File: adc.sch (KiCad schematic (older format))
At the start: 19 parts, among them J15 Conn_01x04_Male, U22 AD7960BCPZ-RL7, U23 OPA325

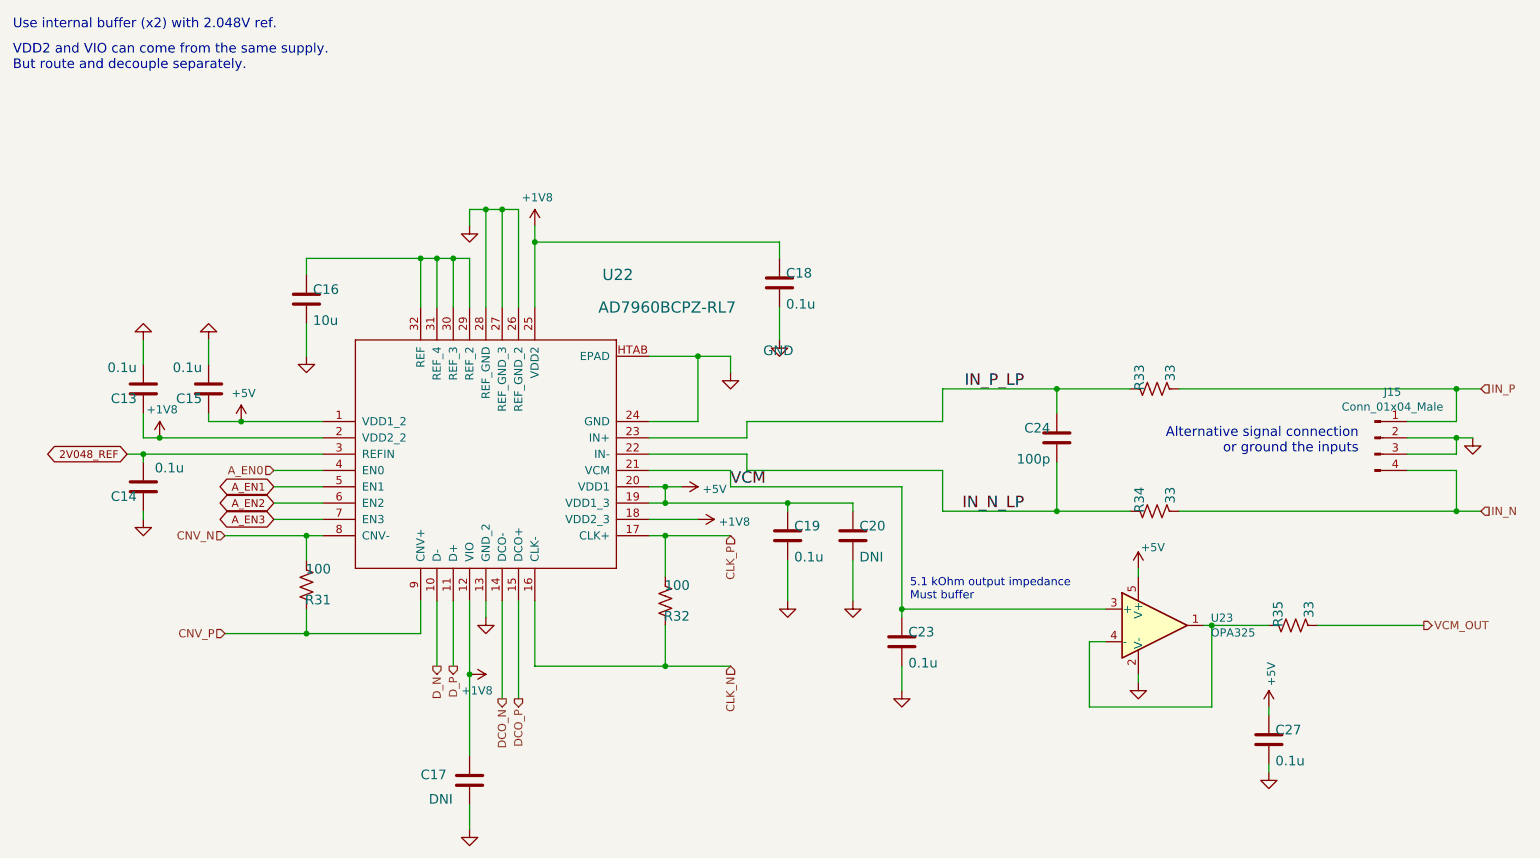
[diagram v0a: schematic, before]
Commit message: moved DCO 7960 signals to dedicated input clock routes
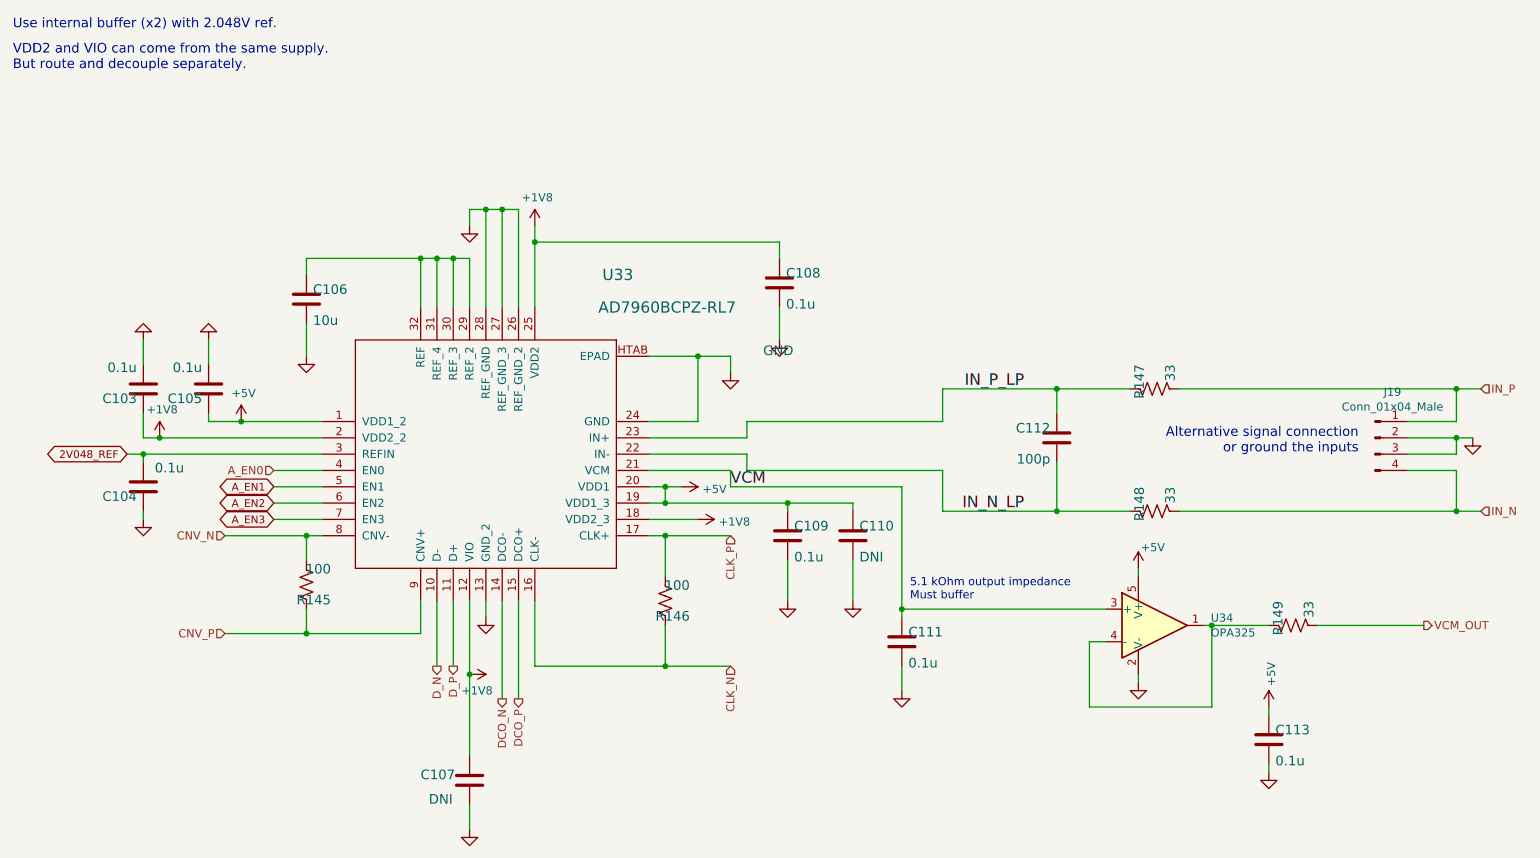
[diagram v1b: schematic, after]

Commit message: added Unique ID chip
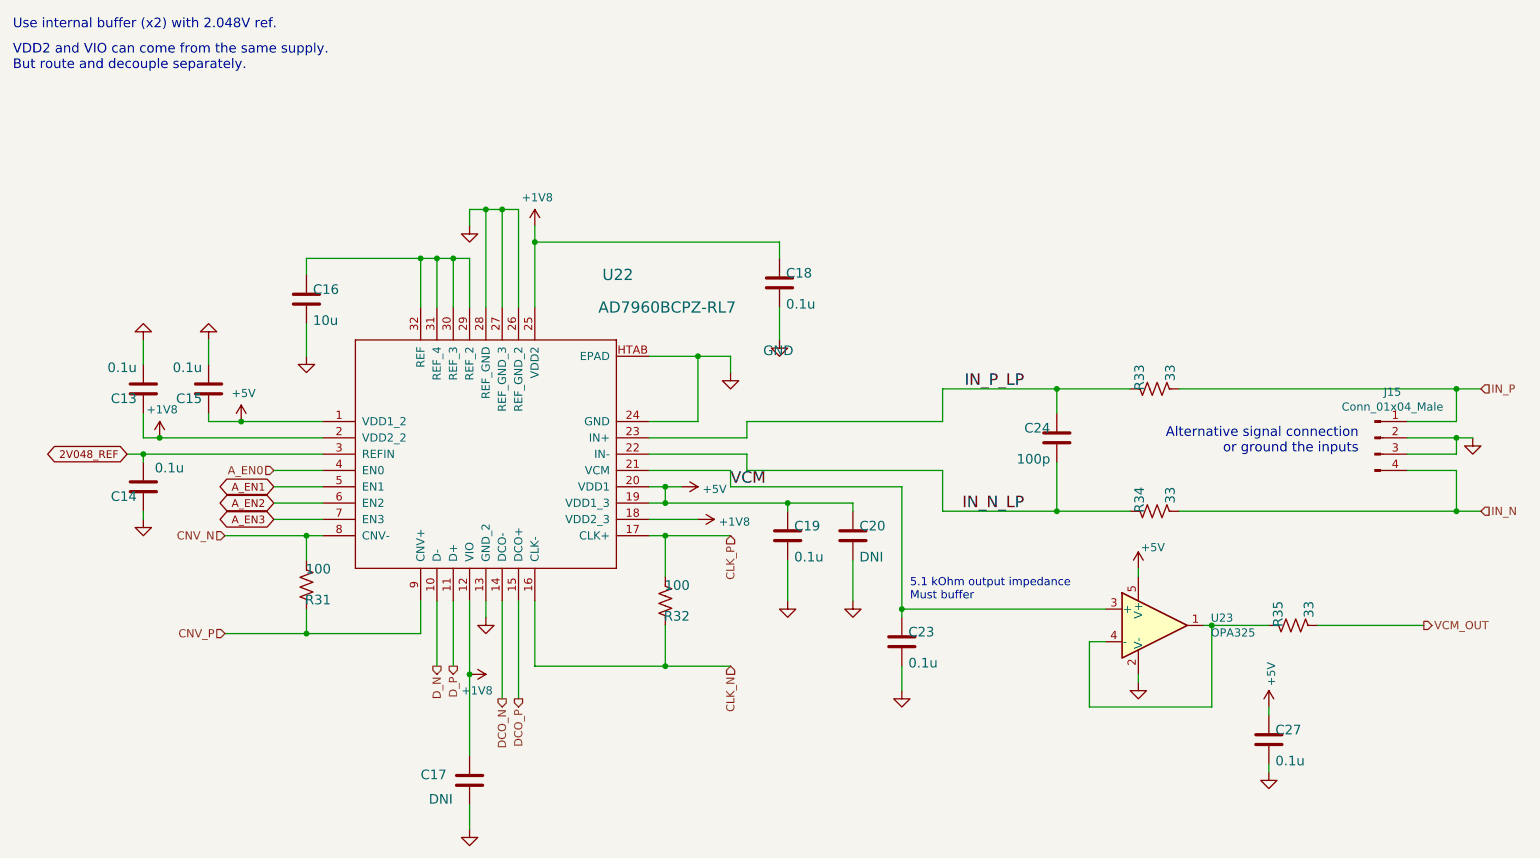
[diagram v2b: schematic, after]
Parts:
- J15: footprint (none) -> Connector_PinHeader_2.54mm:PinHeader_1x04_P2.54mm_Vertical_SMD_Pin1Left; Manf# (none) -> 54201-G0804LF
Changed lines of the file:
@@
 $Descr A 11000 8500
 encoding utf-8
-Sheet 10 18
+Sheet 6 18
 Title ""
 Date ""
@@
 AR Path="/60BF7757/B0DC2316" Ref="C69"  Part="1"
 AR Path="/60C1F416/B0DC2316" Ref="C112"  Part="1"
-F 0 "C112" H 7090 3725 59  0000 L BNN
+F 0 "C24" H 7090 3725 59  0000 L BNN
 F 1 "100p" H 7090 3535 59  0000 L BNN
 F 2 "Capacitor_SMD:C_0603_1608Metric" H 7050 3700 50  0001 C CNN
@@
 AR Path="/60BF7757/B996151F" Ref="R140"  Part="1"
 AR Path="/60C1F416/B996151F" Ref="R145"  Part="1"
-F 0 "R145" H 2300 4659 59  0000 L BNN
+F 0 "R31" H 2300 4659 59  0000 L BNN
 F 1 "100" H 2300 4470 59  0000 L BNN
 F 2 "Resistor_SMD:R_0603_1608Metric" H 2450 4600 50  0001 C CNN
@@
 AR Path="/60BF7757/56DFCCD0" Ref="C65"  Part="1"
 AR Path="/60C1F416/56DFCCD0" Ref="C108"  Part="1"
-F 0 "C108" H 5390 2775 59  0000 L BNN
+F 0 "C18" H 5390 2775 59  0000 L BNN
 F 1 "0.1u" H 5390 2585 59  0000 L BNN
 F 2 "Capacitor_SMD:C_0603_1608Metric" H 5350 2750 50  0001 C CNN
@@
 AR Path="/60BF7757/BF33D434" Ref="R141"  Part="1"
 AR Path="/60C1F416/BF33D434" Ref="R146"  Part="1"
-F 0 "R146" H 4500 4759 59  0000 L BNN
+F 0 "R32" H 4500 4759 59  0000 L BNN
 F 1 "100" H 4500 4570 59  0000 L BNN
 F 2 "Resistor_SMD:R_0603_1608Metric" H 4650 4700 50  0001 C CNN
@@
 AR Path="/60BF7757/C9238E33" Ref="C66"  Part="1"
 AR Path="/60C1F416/C9238E33" Ref="C109"  Part="1"
-F 0 "C109" H 5440 4325 59  0000 L BNN
+F 0 "C19" H 5440 4325 59  0000 L BNN
 F 1 "0.1u" H 5440 4135 59  0000 L BNN
 F 2 "Capacitor_SMD:C_0603_1608Metric" H 5400 4300 50  0001 C CNN
@@
 AR Path="/60BF7757/E612D2BB" Ref="C67"  Part="1"
 AR Path="/60C1F416/E612D2BB" Ref="C110"  Part="1"
-F 0 "C110" H 5840 4325 59  0000 L BNN
+F 0 "C20" H 5840 4325 59  0000 L BNN
 F 1 "DNI" H 5840 4135 59  0000 L BNN
 F 2 "Capacitor_SMD:C_0603_1608Metric" H 5800 4300 50  0001 C CNN
@@
 AR Path="/60BF7757/1FADEAAB" Ref="C60"  Part="1"
 AR Path="/60C1F416/1FADEAAB" Ref="C103"  Part="1"
-F 0 "C103" H 1490 3425 59  0000 L BNN
+F 0 "C13" H 1490 3425 59  0000 L BNN
 F 1 "0.1u" H 1490 3235 59  0000 L BNN
 F 2 "Capacitor_SMD:C_0603_1608Metric" H 1450 3400 50  0001 C CNN
@@
 AR Path="/60BF7757/9D5B9004" Ref="C62"  Part="1"
 AR Path="/60C1F416/9D5B9004" Ref="C105"  Part="1"
-F 0 "C105" H 1890 3425 59  0000 L BNN
+F 0 "C15" H 1890 3425 59  0000 L BNN
 F 1 "0.1u" H 1890 3235 59  0000 L BNN
 F 2 "Capacitor_SMD:C_0603_1608Metric" H 1850 3400 50  0001 C CNN
@@
 AR Path="/60BF7757/87DF8B8E" Ref="R142"  Part="1"
 AR Path="/60C1F416/87DF8B8E" Ref="R147"  Part="1"
-F 0 "R147" H 7500 3459 59  0000 L BNN
+F 0 "R33" H 7500 3459 59  0000 L BNN
 F 1 "33" H 7500 3270 59  0000 L BNN
 F 2 "Resistor_SMD:R_0603_1608Metric" H 7650 3400 50  0001 C CNN
@@
 AR Path="/60BF7757/BFC3FA38" Ref="R143"  Part="1"
 AR Path="/60C1F416/BFC3FA38" Ref="R148"  Part="1"
-F 0 "R148" H 7500 4209 59  0000 L BNN
+F 0 "R34" H 7500 4209 59  0000 L BNN
 F 1 "33" H 7500 4020 59  0000 L BNN
 F 2 "Resistor_SMD:R_0603_1608Metric" H 7650 4150 50  0001 C CNN
@@
 AR Path="/60BF7757/E8572435" Ref="C64"  Part="1"
 AR Path="/60C1F416/E8572435" Ref="C107"  Part="1"
-F 0 "C107" H 3150 5800 59  0000 L BNN
+F 0 "C17" H 3150 5800 59  0000 L BNN
 F 1 "DNI" H 3200 5650 59  0000 L BNN
 F 2 "Capacitor_SMD:C_0603_1608Metric" H 3450 5800 50  0001 C CNN
@@
 AR Path="/60BF7757/70C280EF" Ref="U31"  Part="1"
 AR Path="/60C1F416/70C280EF" Ref="U33"  Part="1"
-F 0 "U33" H 4264 4859 69  0000 L BNN
+F 0 "U22" H 4264 4859 69  0000 L BNN
 F 1 "AD7960BCPZ-RL7" H 4239 4659 69  0000 L BNN
 F 2 "adc_dac_v1:CP_32_7" H 3550 3800 50  0001 C CNN
@@
 AR Path="/60BF7757/32508C8E" Ref="C63"  Part="1"
 AR Path="/60C1F416/32508C8E" Ref="C106"  Part="1"
-F 0 "C106" H 2490 2875 59  0000 L BNN
+F 0 "C16" H 2490 2875 59  0000 L BNN
 F 1 "10u" H 2490 2685 59  0000 L BNN
 F 2 "Capacitor_SMD:C_0603_1608Metric" H 2450 2850 50  0001 C CNN
@@
 AR Path="/60BF7757/60CEDBBA" Ref="U32"  Part="1"
 AR Path="/60C1F416/60CEDBBA" Ref="U34"  Part="1"
-F 0 "U34" H 7994 4896 50  0000 L CNN
+F 0 "U23" H 7994 4896 50  0000 L CNN
 F 1 "OPA325" H 7994 4805 50  0000 L CNN
 F 2 "Package_TO_SOT_SMD:SOT-23-5" H 7550 4650 50  0001 L CNN
@@
 AR Path="/60BF7757/60D076A5" Ref="R144"  Part="1"
 AR Path="/60C1F416/60D076A5" Ref="R149"  Part="1"
-F 0 "R149" H 8350 4909 59  0000 L BNN
+F 0 "R35" H 8350 4909 59  0000 L BNN
 F 1 "33" H 8350 4720 59  0000 L BNN
 F 2 "Resistor_SMD:R_0603_1608Metric" H 8500 4850 50  0001 C CNN
@@
 AR Path="/60BF7757/60D0F62A" Ref="C102"  Part="1"
 AR Path="/60C1F416/60D0F62A" Ref="C113"  Part="1"
-F 0 "C113" H 8390 5575 59  0000 L BNN
+F 0 "C27" H 8390 5575 59  0000 L BNN
 F 1 "0.1u" H 8390 5385 59  0000 L BNN
 F 2 "Capacitor_SMD:C_0603_1608Metric" H 8350 5550 50  0001 C CNN
@@
 AR Path="/60BF7757/60D49EBB" Ref="C61"  Part="1"
 AR Path="/60C1F416/60D49EBB" Ref="C104"  Part="1"
-F 0 "C104" H 1490 4025 59  0000 L BNN
+F 0 "C14" H 1490 4025 59  0000 L BNN
 F 1 "0.1u" H 1200 3850 59  0000 L BNN
 F 2 "Capacitor_SMD:C_0603_1608Metric" H 1450 4000 50  0001 C CNN
@@
 AR Path="/60BF7757/60D51F18" Ref="C68"  Part="1"
 AR Path="/60C1F416/60D51F18" Ref="C111"  Part="1"
-F 0 "C111" H 6140 4975 59  0000 L BNN
+F 0 "C23" H 6140 4975 59  0000 L BNN
 F 1 "0.1u" H 6140 4785 59  0000 L BNN
 F 2 "Capacitor_SMD:C_0603_1608Metric" H 6100 4950 50  0001 C CNN
@@
 AR Path="/60BF7757/628E78F9" Ref="J18"  Part="1"
 AR Path="/60C1F416/628E78F9" Ref="J19"  Part="1"
-F 0 "J19" H 9108 3981 50  0000 C CNN
+F 0 "J15" H 9108 3981 50  0000 C CNN
 F 1 "Conn_01x04_Male" H 9108 3890 50  0000 C CNN
-F 2 "" H 9000 3700 50  0001 C CNN
+F 2 "Connector_PinHeader_2.54mm:PinHeader_1x04_P2.54mm_Vertical_SMD_Pin1Left" H 9000 3700 50  0001 C CNN
 F 3 "~" H 9000 3700 50  0001 C CNN
+F 4 "54201-G0804LF" H 9000 3700 50  0001 C CNN "Manf#"
 	1    9000 3700
 	1    0    0    -1
